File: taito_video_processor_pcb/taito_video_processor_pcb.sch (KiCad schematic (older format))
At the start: 343 parts, among them J1 14pin, J19 2pin, J2 14pin, J3 50pin, J6 50pin, Q1 2N3904, Q2 2N3904, Q3 2N3904, Q4 2N3904, Q5 2N3904, Q6 2N3904, Q7 2N3904, Q8 2N3905, SW1 SW_Push, U1 245_1, U10 4116, U100 LS00, U101 LS08, U102 LS10, U103 LS00, U104 157_1, U105 299_1, U106 299_1, U107 299_1, U108 299_1, U109 299_1, U11 4116, U110 299_1, U12 4116, U13 4116, U14 4116, U15 4116, U16 4116, U17 4116, U18 68A45, U19 86_2, U2 245_1, U20 86_1, U21 157_1, U22 LS32, U23 161_1, U24 LS04, U25 374_1, U26 4116, U27 4116, U28 4116, U29 4116, U3 2114, U30 4116, U31 4116, U32 4116, U33 4116, U34 LS374, U35 153_1, U36 LS74, U37 LS08, U38 74S113, U39 LS04, U4 2114, U40 7417, U41 4116, U42 4116, U43 4116, U44 4116, U45 4116, U46 4116, U47 4116, U48 4116, U49 LS32, U5 157_1, U50 86_3, U51 LS86, U52 153_1, U53 153_1, U54 153_1, U55 157_1, U56 2148_1, U57 2148_2, U58 7417, U59 4116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

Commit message: Completed the BOM
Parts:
- R11, R12, R22, R23, R24, R25, R26, R27, R9: value ? -> 33
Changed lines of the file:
@@
 P 21225 6600
 F 0 "R9" V 21300 6600 50  0000 L CNN
-F 1 "?" V 21300 6475 50  0000 L CNN
+F 1 "33" V 21300 6475 50  0000 L CNN
 F 2 "taito_video_processor_pcb:GenericComp" V 21265 6590 50  0001 C CNN
 F 3 "~" H 21225 6600 50  0001 C CNN
@@
 P 22050 8325
 F 0 "R12" V 21975 8250 50  0000 L CNN
-F 1 "?" V 22150 8300 50  0000 L CNN
+F 1 "33" V 22150 8300 50  0000 L CNN
 F 2 "taito_video_processor_pcb:GenericComp" V 22090 8315 50  0001 C CNN
 F 3 "~" H 22050 8325 50  0001 C CNN
@@
 U 1 1 7974371E
 P 8525 3425
-F 0 "R11" V 8600 3400 50  0000 L CNN
-F 1 "?" V 8600 3325 50  0000 L CNN
+F 0 "R11" V 8600 3425 50  0000 L CNN
+F 1 "33" V 8600 3300 50  0000 L CNN
 F 2 "taito_video_processor_pcb:GenericComp" V 8565 3415 50  0001 C CNN
 F 3 "~" H 8525 3425 50  0001 C CNN
@@
 U 1 1 86FB270C
 P 8525 3275
-F 0 "R24" V 8600 3250 50  0000 L CNN
-F 1 "?" V 8600 3175 50  0000 L CNN
+F 0 "R24" V 8600 3275 50  0000 L CNN
+F 1 "33" V 8600 3150 50  0000 L CNN
 F 2 "taito_video_processor_pcb:GenericComp" V 8565 3265 50  0001 C CNN
 F 3 "~" H 8525 3275 50  0001 C CNN
@@
 U 1 1 877E85CB
 P 8525 2400
-F 0 "R22" V 8600 2375 50  0000 L CNN
-F 1 "?" V 8600 2300 50  0000 L CNN
+F 0 "R22" V 8600 2400 50  0000 L CNN
+F 1 "33" V 8600 2275 50  0000 L CNN
 F 2 "taito_video_processor_pcb:GenericComp" V 8565 2390 50  0001 C CNN
 F 3 "~" H 8525 2400 50  0001 C CNN
@@
 U 1 1 8801C4A9
 P 8525 2550
-F 0 "R23" V 8600 2525 50  0000 L CNN
-F 1 "?" V 8600 2450 50  0000 L CNN
+F 0 "R23" V 8600 2550 50  0000 L CNN
+F 1 "33" V 8600 2425 50  0000 L CNN
 F 2 "taito_video_processor_pcb:GenericComp" V 8565 2540 50  0001 C CNN
 F 3 "~" H 8525 2550 50  0001 C CNN
@@
 U 1 1 888576CE
 P 8525 4150
-F 0 "R26" V 8600 4125 50  0000 L CNN
-F 1 "?" V 8600 4050 50  0000 L CNN
+F 0 "R26" V 8600 4150 50  0000 L CNN
+F 1 "33" V 8600 4025 50  0000 L CNN
 F 2 "taito_video_processor_pcb:GenericComp" V 8565 4140 50  0001 C CNN
 F 3 "~" H 8525 4150 50  0001 C CNN
@@
 U 1 1 8885EA87
 P 8525 4300
-F 0 "R27" V 8600 4275 50  0000 L CNN
-F 1 "?" V 8600 4200 50  0000 L CNN
+F 0 "R27" V 8600 4300 50  0000 L CNN
+F 1 "33" V 8600 4175 50  0000 L CNN
 F 2 "taito_video_processor_pcb:GenericComp" V 8565 4290 50  0001 C CNN
 F 3 "~" H 8525 4300 50  0001 C CNN
@@
 U 1 1 88860321
 P 8525 5025
-F 0 "R25" V 8600 5000 50  0000 L CNN
-F 1 "?" V 8600 4925 50  0000 L CNN
+F 0 "R25" V 8600 5025 50  0000 L CNN
+F 1 "33" V 8600 4900 50  0000 L CNN
 F 2 "taito_video_processor_pcb:GenericComp" V 8565 5015 50  0001 C CNN
 F 3 "~" H 8525 5025 50  0001 C CNN

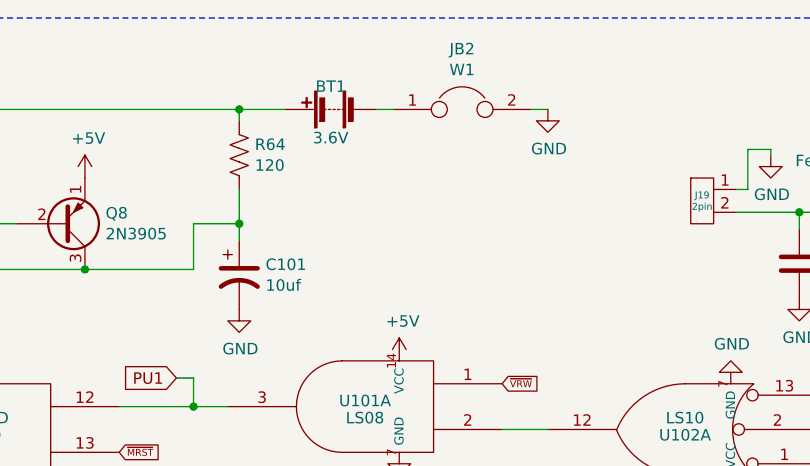
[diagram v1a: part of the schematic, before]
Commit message: Fixed upper left mounting hole and added CR2032 battery to PCB
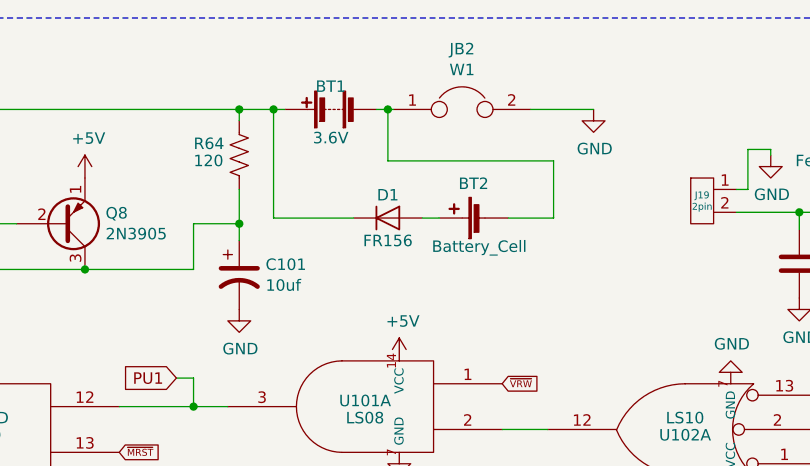
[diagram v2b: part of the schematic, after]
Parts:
- added BT2: Battery_Cell, taito_video_processor_pcb:CR2032, symbol Device:Battery_Cell
- added D1: FR156, taito_video_processor_pcb:GenericComp, symbol Device:D
- U67: footprint (none) -> Star_Wars_Vector_PCB:DIP14
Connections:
- net at BT1.1 (+), R64.1, R65.2: now also D1.1 (K)
- net at BT1.2 (-), JB2.1: now also BT2.2 (-)
- new net: BT2.1 (+), D1.2 (A)
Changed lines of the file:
@@
 U 1 1 6131D39F
 P 13350 1300
-F 0 "R64" H 13418 1346 50  0000 L CNN
-F 1 "120" H 13418 1255 50  0000 L CNN
+F 0 "R64" H 13150 1350 50  0000 L CNN
+F 1 "120" H 13150 1275 50  0000 L CNN
 F 2 "taito_video_processor_pcb:GenericComp" V 13390 1290 50  0001 C CNN
 F 3 "~" H 13350 1300 50  0001 C CNN
@@
 Connection ~ 13350 1100
 Wire Wire Line
-	13350 1100 13550 1100
+	13350 1100 13500 1100
 Wire Wire Line
 	13150 1800 13150 1600
@@
 $EndComp
 Wire Wire Line
-	14025 1100 13950 1100
+	14025 1100 14000 1100
 $Comp
 L power:GND #PWR0157
 U 1 1 61419144
-P 14700 1100
-F 0 "#PWR0157" H 14700 850 50  0001 C CNN
-F 1 "GND" H 14705 927 50  0000 C CNN
-F 2 "" H 14700 1100 50  0001 C CNN
-F 3 "" H 14700 1100 50  0001 C CNN
-	1    14700 1100
+P 14900 1100
+F 0 "#PWR0157" H 14900 850 50  0001 C CNN
+F 1 "GND" H 14905 927 50  0000 C CNN
+F 2 "" H 14900 1100 50  0001 C CNN
+F 3 "" H 14900 1100 50  0001 C CNN
+	1    14900 1100
 	1    0    0    -1
 $EndComp
 Wire Wire Line
-	14700 1100 14625 1100
-Wire Wire Line
 	11800 1800 12675 1800
 Connection ~ 12675 1800
@@
 F 0 "U67" H 10500 14675 50  0000 L CNN
 F 1 "LS32" H 10500 14575 50  0000 L CNN
-F 2 "" H 10550 14625 50  0001 C CNN
+F 2 "Star_Wars_Vector_PCB:DIP14" H 10550 14625 50  0001 C CNN
 F 3 "" H 10550 14625 50  0001 C CNN
 	1    10550 14625
@@
 F 0 "U67" H 10525 19475 50  0000 C CNN
 F 1 "LS32" H 10525 19400 50  0000 C CNN
-F 2 "" H 10525 19450 50  0001 C CNN
+F 2 "Star_Wars_Vector_PCB:DIP14" H 10525 19450 50  0001 C CNN
 F 3 "" H 10525 19450 50  0001 C CNN
 	2    10525 19450
@@
 	32000 17225 32000 17175
 Connection ~ 31625 17225
+$Comp
+L Device:D D1
+U 1 1 62E409E3
+P 14000 1575
+F 0 "D1" H 14000 1675 50  0000 C CNN
+F 1 "FR156" H 14000 1475 50  0000 C CNN
+F 2 "taito_video_processor_pcb:GenericComp" H 14000 1575 50  0001 C CNN
+F 3 "~" H 14000 1575 50  0001 C CNN
+	1    14000 1575
+	1    0    0    -1
+$EndComp
+$Comp
+L Device:Battery_Cell BT2
+U 1 1 62E4E0EC
+P 14425 1575
+F 0 "BT2" V 14575 1625 50  0000 C CNN
+F 1 "Battery_Cell" V 14300 1600 50  0000 C CNN
+F 2 "taito_video_processor_pcb:CR2032" V 14425 1635 50  0001 C CNN
+F 3 "~" V 14425 1635 50  0001 C CNN
+	1    14425 1575
+	0    -1   -1   0
+$EndComp
+Wire Wire Line
+	14525 1575 14725 1575
+Wire Wire Line
+	14225 1575 14150 1575
+Wire Wire Line
+	13850 1575 13500 1575
+Wire Wire Line
+	13500 1575 13500 1100
+Connection ~ 13500 1100
+Wire Wire Line
+	13500 1100 13550 1100
+Wire Wire Line
+	14625 1100 14900 1100
+Wire Wire Line
+	14000 1100 14000 1325
+Wire Wire Line
+	14000 1325 14725 1325
+Wire Wire Line
+	14725 1325 14725 1575
+Connection ~ 14000 1100
+Wire Wire Line
+	14000 1100 13950 1100
 $EndSCHEMATC

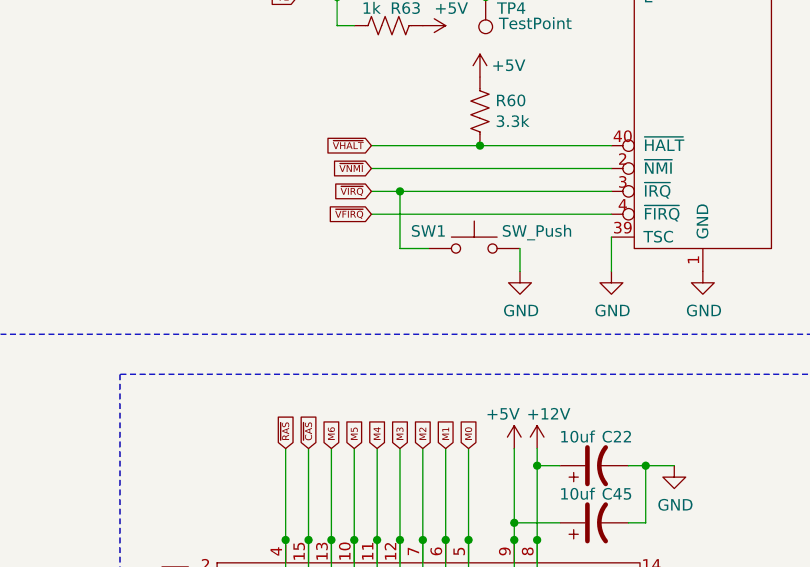
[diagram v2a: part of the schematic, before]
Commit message: Added alternative switch
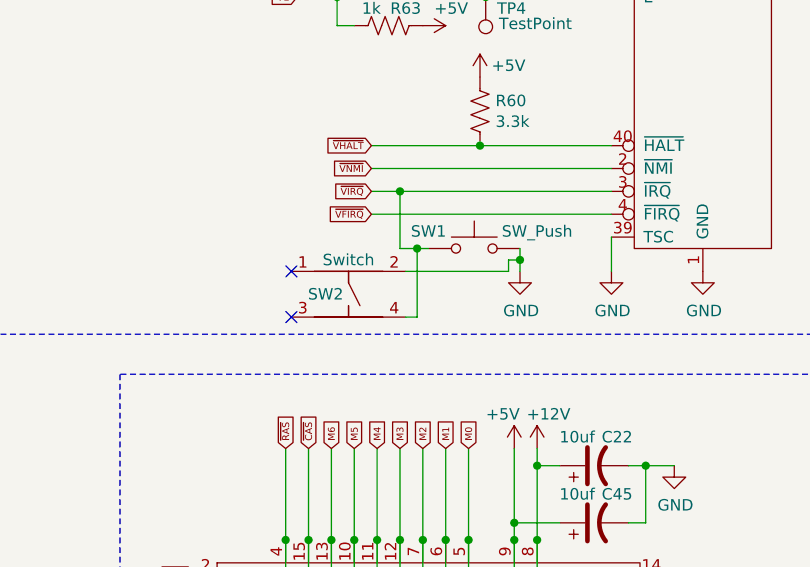
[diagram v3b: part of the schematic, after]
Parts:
- added SW2: Switch, taito_video_processor_pcb:Pushbutton, symbol taito_pcb:Switch
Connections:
- net GND: now also SW2.2
- net ~VIRQ: now also SW2.4
- no-connect marks 92 -> 94
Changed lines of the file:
@@
 $EndComp
 Wire Wire Line
-	2900 10450 2775 10450
-Wire Wire Line
 	2775 10450 2775 10200
 Connection ~ 2775 10200
@@
 	1    0    0    -1
 $EndComp
-Wire Wire Line
-	3300 10450 3300 10550
 Wire Notes Line
 	775  6100 775  10825
@@
 Wire Wire Line
 	14000 1100 13950 1100
+$Comp
+L taito_pcb:Switch SW2
+U 1 1 621F6DC1
+P 2550 10650
+F 0 "SW2" H 2450 10650 50  0000 C CNN
+F 1 "Switch" H 2550 10800 50  0000 C CNN
+F 2 "taito_video_processor_pcb:Pushbutton" H 2550 10650 50  0001 C CNN
+F 3 "" H 2550 10650 50  0001 C CNN
+	1    2550 10650
+	1    0    0    -1
+$EndComp
+NoConn ~ 2300 10550
+NoConn ~ 2300 10750
+Wire Wire Line
+	3300 10450 3300 10500
+Wire Wire Line
+	2775 10450 2850 10450
+Wire Wire Line
+	2800 10550 3250 10550
+Wire Wire Line
+	3250 10550 3250 10500
+Wire Wire Line
+	3250 10500 3300 10500
+Connection ~ 3300 10500
+Wire Wire Line
+	3300 10500 3300 10550
+Wire Wire Line
+	2850 10450 2850 10750
+Wire Wire Line
+	2850 10750 2800 10750
+Connection ~ 2850 10450
+Wire Wire Line
+	2850 10450 2900 10450
 $EndSCHEMATC
